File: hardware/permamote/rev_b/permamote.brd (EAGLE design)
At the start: 27 x 60 mm, 125 parts, among them J1 TC2030-JLINK-NL, J5 MICRO_USB_B_HIROSE_ZX62R-B-5P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, Q1 PMDXB950UPEL, Q10 PMDXB950UPEL, Q2 PMDXB950UPEL, Q3 PMDXB950UPEL, Q4 PMDXB950UPEL, Q5 PMDXB950UPEL, Q6 PMDXB950UPEL, Q7 PMDXB950UPEL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

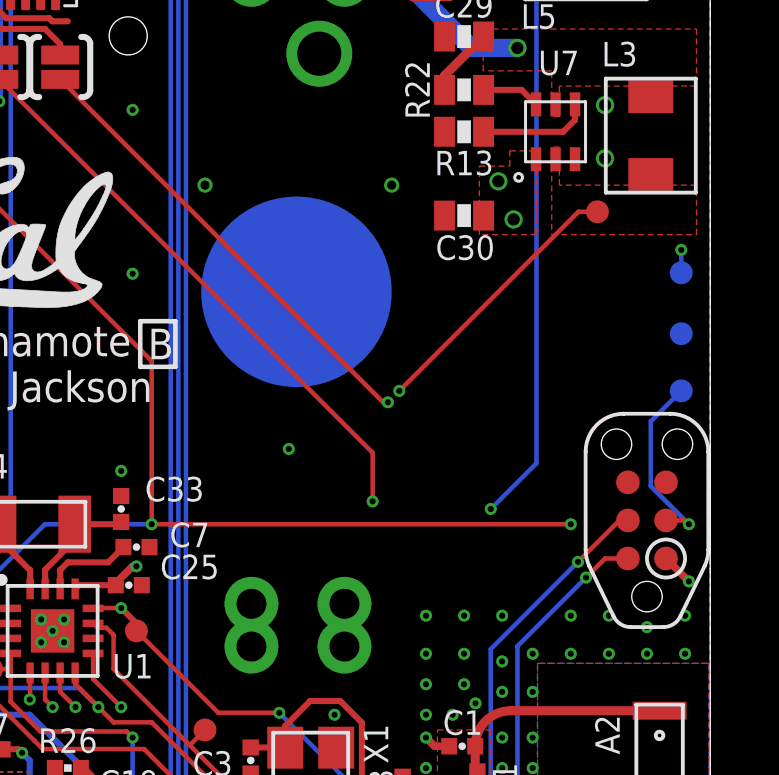
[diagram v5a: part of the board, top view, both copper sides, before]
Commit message: clean up vcc/gnd connections
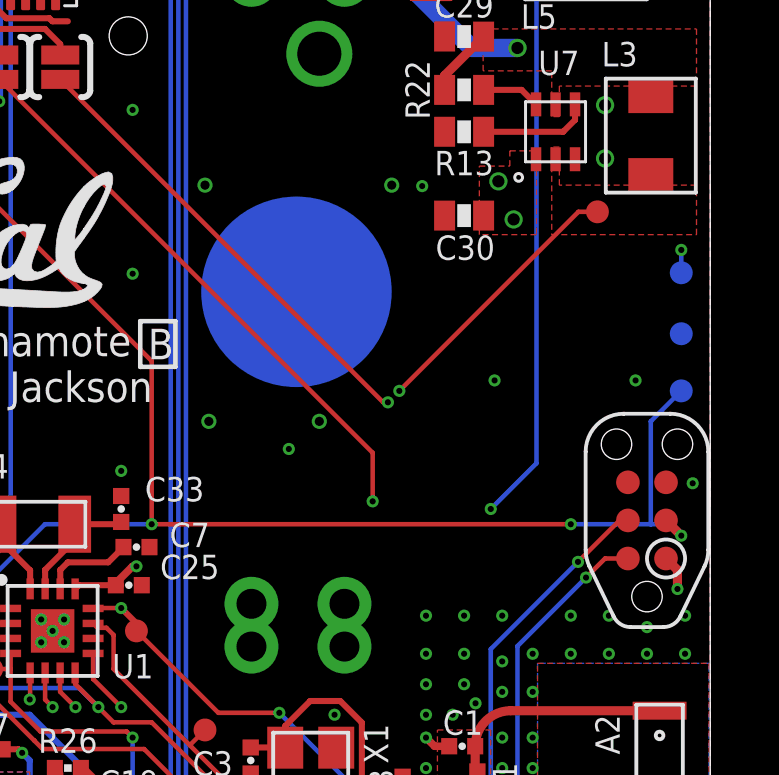
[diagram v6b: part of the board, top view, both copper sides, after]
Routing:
- net VCC: track 54.8 -> 67.5 mm, vias 25 -> 29
- net N$1: track 6.22 -> 0.00 mm, vias 2 -> 0
- net !RST: track 66.3 -> 65.6 mm
- net GND: vias 105 -> 109
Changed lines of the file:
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@@
 <wire x1="19.812" y1="0.6858" x2="21.082" y2="0.6858" width="0.254" layer="1"/>
 <contactref element="U12" pad="3"/>
+<via x="17.399" y="42.005" extent="1-16" drill="0.2032"/>
+<via x="19.812" y="35.528" extent="1-16" drill="0.2032"/>
+<via x="24.511" y="35.528" extent="1-16" drill="0.2032"/>
+<via x="26.416" y="32.099" extent="1-16" drill="0.2032"/>
 </signal>
 <signal name="N$8">
@@
 <wire x1="6.93293125" y1="21.336" x2="6.93293125" y2="21.76906875" width="0.254" layer="1"/>
 <wire x1="6.93293125" y1="21.76906875" x2="6.604" y2="22.098" width="0.254" layer="1"/>
-<via x="26.289" y="28.829" extent="1-16" drill="0.2032"/>
+<via x="25.908" y="28.575" extent="1-16" drill="0.2032"/>
 <wire x1="16.129" y1="19.304" x2="16.129" y2="18.86" width="0.254" layer="1"/>
 <wire x1="16.33093125" y1="2.286" x2="16.33093125" y2="2.61493125" width="0.254" layer="1"/>
@@
 <wire x1="9.017" y1="10.922" x2="9.59993125" y2="10.922" width="0.2032" layer="1"/>
 <wire x1="9.59993125" y1="10.922" x2="9.652" y2="10.86993125" width="0.2032" layer="1"/>
-<wire x1="25.527" y1="29.591" x2="26.289" y2="28.829" width="0.254" layer="1"/>
 <wire x1="21.992" y1="13.86" x2="21.717" y2="13.585" width="0.4064" layer="1"/>
 <wire x1="21.717" y1="13.585" x2="21.717" y2="13.335" width="0.4064" layer="1"/>
@@
 <wire x1="8.89" y1="53.54193125" x2="9.34593125" y2="53.54193125" width="0.1524" layer="1"/>
 <wire x1="9.34593125" y1="53.54193125" x2="9.525" y2="53.721" width="0.1524" layer="1"/>
+<via x="16.383" y="42.037" extent="1-16" drill="0.3048"/>
+<wire x1="16.383" y1="42.037" x2="10.16" y2="42.037" width="0.8128" layer="2"/>
+<via x="10.16" y="42.037" extent="1-16" drill="0.3048"/>
+<wire x1="13.97" y1="34.163" x2="10.287" y2="34.163" width="0.8128" layer="2"/>
+<via x="13.97" y="34.163" extent="1-16" drill="0.3048"/>
+<wire x1="13.97" y1="34.163" x2="15.748" y2="34.163" width="0.8128" layer="15"/>
+<wire x1="15.748" y1="34.163" x2="16.383" y2="33.528" width="0.8128" layer="15"/>
+<via x="10.287" y="34.163" extent="1-16" drill="0.3048"/>
+<wire x1="25.908" y1="28.575" x2="25.908" y2="29.21" width="0.3048" layer="1"/>
+<wire x1="25.908" y1="29.21" x2="25.527" y2="29.591" width="0.3048" layer="1"/>
+<wire x1="9.525" y1="53.721" x2="14.097" y2="59.309" width="0" layer="19" extent="1-1"/>
+<wire x1="1.27" y1="45.5731" x2="8.89" y2="53.54193125" width="0" layer="19" extent="1-1"/>
+<wire x1="10.16" y1="42.037" x2="1.27" y2="44.831" width="0" layer="19" extent="1-2"/>
+<wire x1="19.446" y1="41.021" x2="16.383" y2="42.037" width="0" layer="19" extent="1-1"/>
+<wire x1="20.447" y1="40.894" x2="19.446" y2="41.021" width="0" layer="19" extent="1-1"/>
+<wire x1="19.939" y1="42.164" x2="19.446" y2="41.021" width="0" layer="19" extent="1-1"/>
+<wire x1="21.194" y1="42.9" x2="19.939" y2="42.164" width="0" layer="19" extent="1-1"/>
+<wire x1="26.035" y1="39.878" x2="20.447" y2="40.894" width="0" layer="19" extent="1-1"/>
+<wire x1="15.748" y1="34.163" x2="19.446" y2="41.021" width="0" layer="19" extent="1-15"/>
+<wire x1="7.874" y1="29.33065" x2="10.287" y2="34.163" width="0" layer="19" extent="1-2"/>
+<wire x1="2.032" y1="29.38906875" x2="5.83" y2="28.578" width="0" layer="19" extent="1-1"/>
+<wire x1="2.032" y1="23.876" x2="2.032" y2="29.38906875" width="0" layer="19" extent="1-1"/>
+<wire x1="6.02106875" y1="22.606" x2="2.55193125" y2="23.232" width="0" layer="19" extent="1-1"/>
+<wire x1="5.334" y1="17.272" x2="6.67893125" y2="18.542" width="0" layer="19" extent="1-1"/>
+<wire x1="5.759" y1="16.033" x2="4.909" y2="16.733" width="0" layer="19" extent="1-1"/>
+<wire x1="10.16" y1="19.05" x2="7.112" y2="19.304" width="0" layer="19" extent="1-2"/>
+<wire x1="8.426" y1="11.461" x2="6.35" y2="15.494" width="0" layer="19" extent="1-1"/>
+<wire x1="17.242" y1="13.36" x2="16.742" y2="18.86" width="0" layer="19" extent="1-1"/>
+<wire x1="21.717" y1="13.335" x2="17.242" y2="13.36" width="0" layer="19" extent="1-1"/>
+<wire x1="23.242" y1="16.86" x2="21.992" y2="13.86" width="0" layer="19" extent="1-1"/>
+<wire x1="23.242" y1="19.36" x2="23.242" y2="16.86" width="0" layer="19" extent="1-1"/>
+<wire x1="23.44293125" y1="7.747" x2="21.64206875" y2="11.811" width="0" layer="19" extent="1-1"/>
+<wire x1="22.777" y1="1.682" x2="21.927" y2="2.382" width="0" layer="19" extent="1-1"/>
+<wire x1="17.78" y1="3.37693125" x2="21.209" y2="2.794" width="0" layer="19" extent="1-1"/>
+<wire x1="25.908" y1="28.575" x2="24.249" y2="20.42" width="0" layer="19" extent="1-1"/>
 </signal>
 <signal name="N$12">
@@
 <via x="22.742" y="16.61" extent="1-16" drill="0.1524"/>
 <contactref element="SJ3" pad="1"/>
-<wire x1="22.352" y1="30.734" x2="26.289" y2="30.734" width="0.1524" layer="15"/>
-<via x="26.289" y="30.734" extent="1-16" drill="0.2032"/>
-<wire x1="26.289" y1="30.734" x2="26.162" y2="30.861" width="0.1524" layer="1"/>
-<wire x1="26.162" y1="30.861" x2="25.527" y2="30.861" width="0.1524" layer="1"/>
+<via x="26.035" y="30.353" extent="1-16" drill="0.2032"/>
 <wire x1="2.032" y1="28.52293125" x2="2.62693125" y2="27.928" width="0.1524" layer="1"/>
 <wire x1="2.62693125" y1="27.928" x2="3.68" y2="27.928" width="0.1524" layer="1"/>
@@
 <wire x1="8.382" y1="36.1751" x2="8.382" y2="30.734" width="0.1524" layer="1"/>
 <wire x1="26.035" y1="35.179" x2="25.019" y2="34.163" width="0.1524" layer="16"/>
-<wire x1="25.019" y1="34.163" x2="25.019" y2="32.004" width="0.1524" layer="16"/>
-<wire x1="25.019" y1="32.004" x2="26.289" y2="30.734" width="0.1524" layer="16"/>
+<wire x1="25.527" y1="30.861" x2="26.035" y2="30.353" width="0.3048" layer="1"/>
+<wire x1="22.352" y1="30.734" x2="25.019" y2="30.734" width="0.1524" layer="16"/>
+<wire x1="25.019" y1="30.734" x2="25.654" y2="30.734" width="0.1524" layer="16"/>
+<wire x1="25.654" y1="30.734" x2="26.035" y2="30.353" width="0.1524" layer="16"/>
+<wire x1="25.019" y1="34.163" x2="25.019" y2="30.734" width="0.1524" layer="16"/>
 </signal>
 <signal name="!RTC_IRQ1">
@@
 <wire x1="20.574" y1="20.026" x2="20.574" y2="28.956" width="0.1524" layer="2"/>
 </signal>
-<signal name="N$1">
-<via x="16.383" y="42.037" extent="1-16" drill="0.3048"/>
-<wire x1="16.383" y1="42.037" x2="10.16" y2="42.037" width="0.8128" layer="2"/>
-<via x="10.16" y="42.037" extent="1-16" drill="0.3048"/>
-</signal>
 </signals>

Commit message: add mpn, a few nits
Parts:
- R6, R7: value 10k -> DNP
- flipped TP26 to the top
- flipped TP27 to the top
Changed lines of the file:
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@@
 <?xml version="1.0" encoding="utf-8"?>
 <!DOCTYPE eagle SYSTEM "eagle.dtd">
-<eagle version="9.0.1">
+<eagle version="9.0.0">
 <drawing>
 <settings>
@@
 <wire x1="8.001" y1="37.503" x2="9.171" y2="37.503" width="0.1524" layer="25"/>
 <wire x1="9.171" y1="37.503" x2="9.171" y2="35.979" width="0.1524" layer="25"/>
-<text x="25.527" y="37.084" size="0.8128" layer="26" font="vector" ratio="12" rot="MR180" align="center-right">GND</text>
-<text x="25.527" y="39.116" size="0.8128" layer="26" font="vector" ratio="12" rot="MR180" align="center-right">VCC</text>
+<text x="25.527" y="37.084" size="0.8128" layer="25" font="vector" ratio="12" align="center-right">GND</text>
+<text x="25.527" y="39.116" size="0.8128" layer="25" font="vector" ratio="12" align="center-right">VCC</text>
 <wire x1="0" y1="60" x2="0.5" y2="60" width="0" layer="20"/>
 <wire x1="10.5" y1="60" x2="27" y2="60" width="0" layer="20"/>
@@
 <attribute name="NAME" x="20.193" y="4.318" size="0.8128" layer="25" font="vector" ratio="12" rot="R180" align="bottom-center"/>
 </element>
-<element name="R6" library="passives" package="0402_RES" value="10k" x="1.207" y="23.232" smashed="yes">
+<element name="R6" library="passives" package="0402_RES" value="DNP" x="1.207" y="23.232" smashed="yes">
 <attribute name="DIGIKEY" value="311-10KJRCT-ND " x="2.477" y="23.232" size="1.778" layer="27" display="off"/>
 <attribute name="MPN" value="RC0402JR-0710KL" x="1.207" y="23.232" size="1.778" layer="27" display="off"/>
@@
 <attribute name="VALUE" x="1.207" y="21.835" size="1.016" layer="27" font="vector" ratio="12" align="bottom-center"/>
 </element>
-<element name="R7" library="passives" package="0402_RES" value="10k" x="2.985" y="23.232" smashed="yes" rot="R180">
+<element name="R7" library="passives" package="0402_RES" value="DNP" x="2.985" y="23.232" smashed="yes" rot="R180">
 <attribute name="DIGIKEY" value="311-10KJRCT-ND " x="2.985" y="23.232" size="1.778" layer="27" rot="R180" display="off"/>
 <attribute name="MPN" value="RC0402JR-0710KL" x="2.985" y="23.232" size="1.778" layer="27" rot="R180" display="off"/>
@@
 </element>
 <element name="U$2" library="logos" package="UCB_CAL_200MIL" value="" x="0.635" y="37.846"/>
-<element name="D1" library="permamote" package="SOLAR_HOLES" value="SOLARCELLHOLES" x="25.019" y="53.594" smashed="yes" rot="R270"/>
+<element name="D1" library="permamote" package="SOLAR_HOLES" value="SOLARCELLHOLES" x="25.019" y="53.594" smashed="yes" rot="R270">
+<attribute name="DIGIKEY" value="869-1001-ND" x="25.019" y="53.594" size="1.778" layer="27" rot="R270" display="off"/>
+<attribute name="MPN" value="AM-1454CA" x="25.019" y="53.594" size="1.778" layer="27" rot="R270" display="off"/>
+</element>
 <element name="D2" library="leds" package="1MM_SQ_4PAD" value="SML-LX0404SIUPGUSB" x="15.113" y="58.928" smashed="yes" rot="R90">
 <attribute name="DIGIKEY" value="67-2125-1-ND" x="15.113" y="58.928" size="1.778" layer="27" rot="R90" display="off"/>
@@
 <element name="TP24" library="headers" package="PAD.03X.03" value="TEST-POINT" x="13.843" y="16.764"/>
 <element name="TP25" library="headers" package="PAD.03X.03" value="TEST-POINT" x="23.241" y="41.148"/>
-<element name="TP26" library="headers" package="PAD.03X.03" value="TEST-POINT" x="26.035" y="39.116" rot="MR0"/>
-<element name="TP27" library="headers" package="PAD.03X.03" value="TEST-POINT" x="26.035" y="37.084" rot="MR0"/>
+<element name="TP26" library="headers" package="PAD.03X.03" value="TEST-POINT" x="26.035" y="39.116"/>
+<element name="TP27" library="headers" package="PAD.03X.03" value="TEST-POINT" x="26.035" y="37.084"/>
 <element name="U12" library="chips" package="FN-6" value="TCS34725" x="25.146" y="2.159" smashed="yes">
 <attribute name="DIGIKEY" value="TCS34725FNCT-ND" x="25.146" y="2.159" size="1.778" layer="27" display="off"/>
+<attribute name="MPN" value="TCS34725FN" x="25.146" y="2.159" size="1.778" layer="27" display="off"/>
 <attribute name="NAME" x="26.654" y="4.315" size="0.8128" layer="23" font="vector" ratio="12" rot="R180"/>
 </element>
@@
 <wire x1="24.5364" y1="16.8656" x2="24.96693125" y2="16.43506875" width="0.254" layer="1"/>
 <wire x1="24.96693125" y1="16.43506875" x2="25.146" y2="16.43506875" width="0.254" layer="1"/>
-<wire x1="26.035" y1="39.116" x2="26.035" y2="39.878" width="0.1524" layer="16"/>
+<wire x1="26.035" y1="39.116" x2="26.035" y2="39.878" width="0.1524" layer="1"/>
 <wire x1="24.29993125" y1="19.773" x2="24.29993125" y2="20.36906875" width="0.254" layer="1"/>
 <wire x1="24.29993125" y1="20.36906875" x2="24.249" y2="20.42" width="0.254" layer="1"/>
@@
 <wire x1="25.908" y1="28.575" x2="25.908" y2="29.21" width="0.3048" layer="1"/>
 <wire x1="25.908" y1="29.21" x2="25.527" y2="29.591" width="0.3048" layer="1"/>
-<wire x1="9.525" y1="53.721" x2="14.097" y2="59.309" width="0" layer="19" extent="1-1"/>
-<wire x1="1.27" y1="45.5731" x2="8.89" y2="53.54193125" width="0" layer="19" extent="1-1"/>
-<wire x1="10.16" y1="42.037" x2="1.27" y2="44.831" width="0" layer="19" extent="1-2"/>
-<wire x1="19.446" y1="41.021" x2="16.383" y2="42.037" width="0" layer="19" extent="1-1"/>
-<wire x1="20.447" y1="40.894" x2="19.446" y2="41.021" width="0" layer="19" extent="1-1"/>
-<wire x1="19.939" y1="42.164" x2="19.446" y2="41.021" width="0" layer="19" extent="1-1"/>
-<wire x1="21.194" y1="42.9" x2="19.939" y2="42.164" width="0" layer="19" extent="1-1"/>
-<wire x1="26.035" y1="39.878" x2="20.447" y2="40.894" width="0" layer="19" extent="1-1"/>
-<wire x1="15.748" y1="34.163" x2="19.446" y2="41.021" width="0" layer="19" extent="1-15"/>
-<wire x1="7.874" y1="29.33065" x2="10.287" y2="34.163" width="0" layer="19" extent="1-2"/>
-<wire x1="2.032" y1="29.38906875" x2="5.83" y2="28.578" width="0" layer="19" extent="1-1"/>
-<wire x1="2.032" y1="23.876" x2="2.032" y2="29.38906875" width="0" layer="19" extent="1-1"/>
-<wire x1="6.02106875" y1="22.606" x2="2.55193125" y2="23.232" width="0" layer="19" extent="1-1"/>
-<wire x1="5.334" y1="17.272" x2="6.67893125" y2="18.542" width="0" layer="19" extent="1-1"/>
-<wire x1="5.759" y1="16.033" x2="4.909" y2="16.733" width="0" layer="19" extent="1-1"/>
-<wire x1="10.16" y1="19.05" x2="7.112" y2="19.304" width="0" layer="19" extent="1-2"/>
-<wire x1="8.426" y1="11.461" x2="6.35" y2="15.494" width="0" layer="19" extent="1-1"/>
-<wire x1="17.242" y1="13.36" x2="16.742" y2="18.86" width="0" layer="19" extent="1-1"/>
-<wire x1="21.717" y1="13.335" x2="17.242" y2="13.36" width="0" layer="19" extent="1-1"/>
-<wire x1="23.242" y1="16.86" x2="21.992" y2="13.86" width="0" layer="19" extent="1-1"/>
-<wire x1="23.242" y1="19.36" x2="23.242" y2="16.86" width="0" layer="19" extent="1-1"/>
-<wire x1="23.44293125" y1="7.747" x2="21.64206875" y2="11.811" width="0" layer="19" extent="1-1"/>
-<wire x1="22.777" y1="1.682" x2="21.927" y2="2.382" width="0" layer="19" extent="1-1"/>
-<wire x1="17.78" y1="3.37693125" x2="21.209" y2="2.794" width="0" layer="19" extent="1-1"/>
-<wire x1="25.908" y1="28.575" x2="24.249" y2="20.42" width="0" layer="19" extent="1-1"/>
 </signal>
 <signal name="N$12">
